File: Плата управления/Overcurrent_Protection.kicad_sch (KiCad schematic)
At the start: 10 parts, among them U5 INA283, U5 LMV7239M5

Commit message: VER2.0
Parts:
- U5: value INA283 -> INA282
- U5: footprint Package_TO_SOT_SMD:SOT-353_SC-70-5 -> Package_TO_SOT_SMD:SOT-23-5_HandSoldering
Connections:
- net +3.3V: no longer U5.3 (REF2)
- net GND: now also U5.3 (REF2)
- net Shunt_1 renamed Shunt-
- net Shunt_2 renamed Shunt+
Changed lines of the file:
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@@
     (effects (font (size 2.5 2.5) bold) (justify left bottom))
   )
-  (global_label "Shunt_1" (shape input) (at 121.285 113.03 180) (fields_autoplaced)
+  (global_label "Shunt-" (shape input) (at 121.285 113.03 180) (fields_autoplaced)
     (effects (font (size 1.27 1.27)) (justify right))
-    (property "Intersheetrefs" "${INTERSHEET_REFS}" (at 110.8199 113.03 0)
+    (property "Intersheetrefs" "${INTERSHEET_REFS}" (at 113.1833 113.03 0)
       (effects (font (size 1.27 1.27)) (justify right) hide)
     )
   )
-  (global_label "Shunt_2" (shape input) (at 121.285 107.95 180) (fields_autoplaced)
+  (global_label "Shunt+" (shape input) (at 121.285 107.95 180) (fields_autoplaced)
     (effects (font (size 1.27 1.27)) (justify right))
-    (property "Intersheetrefs" "${INTERSHEET_REFS}" (at 110.8199 107.95 0)
+    (property "Intersheetrefs" "${INTERSHEET_REFS}" (at 113.1833 107.95 0)
       (effects (font (size 1.27 1.27)) (justify right) hide)
     )
@@
     )
   )
+  (symbol (lib_id "power:GND") (at 128.905 119.38 0) (unit 1)
+    (in_bom yes) (on_board yes) (dnp no) (fields_autoplaced)
+    (property "Reference" "#PWR047" (at 128.905 125.73 0)
+      (effects (font (size 1.27 1.27)) hide)
+    )
+    (property "Value" "GND" (at 128.905 124.46 0)
+      (effects (font (size 1.27 1.27)))
+    )
+    (property "Footprint" "" (at 128.905 119.38 0)
+      (effects (font (size 1.27 1.27)) hide)
+    )
+    (property "Datasheet" "" (at 128.905 119.38 0)
+      (effects (font (size 1.27 1.27)) hide)
+    )
+    (pin "1")
+    (instances
+      (project "Плата управления"
+        (path "/75f4c67c-bbde-4446-8f82-67797a1b269f/d6b8b9ce-300b-4d22-9d4c-9182eba581b1"
+          (reference "#PWR047") (unit 1)
+        )
+        (path "/75f4c67c-bbde-4446-8f82-67797a1b269f/c91ff3ec-ad20-4326-acd4-2c9dea437172"
+          (reference "#PWR021") (unit 1)
+        )
+      )
+      (project "Силовая плата"
+        (path "/96c6fc92-8ec6-44f7-b0dc-9ad8f1acea09"
+          (reference "#PWR06") (unit 1)
+        )
+        (path "/96c6fc92-8ec6-44f7-b0dc-9ad8f1acea09/1efb5faf-bb82-4ac6-a144-d6576b4720aa"
+          (reference "#PWR015") (unit 1)
+        )
+        (path "/96c6fc92-8ec6-44f7-b0dc-9ad8f1acea09/a27b443f-c036-4fd6-934c-6ea912709de0"
+          (reference "#PWR025") (unit 1)
+        )
+      )
+    )
+  )
   (symbol (lib_id "Amplifier_Current:INA283") (at 128.905 110.49 0) (unit 1)
     (in_bom yes) (on_board yes) (dnp no)
@@
       (effects (font (size 1.27 1.27)))
     )
-    (property "Value" "INA283" (at 133.985 107.95 0)
+    (property "Value" "INA282" (at 133.985 107.95 0)
       (effects (font (size 1.27 1.27)))
     )
@@
     )
   )
-  (symbol (lib_id "power:+3.3V") (at 128.905 119.38 180) (unit 1)
-    (in_bom yes) (on_board yes) (dnp no) (fields_autoplaced)
-    (property "Reference" "#PWR025" (at 128.905 115.57 0)
-      (effects (font (size 1.27 1.27)) hide)
-    )
-    (property "Value" "+3.3V" (at 128.905 124.46 0)
-      (effects (font (size 1.27 1.27)))
-    )
-    (property "Footprint" "" (at 128.905 119.38 0)
-      (effects (font (size 1.27 1.27)) hide)
-    )
-    (property "Datasheet" "" (at 128.905 119.38 0)
-      (effects (font (size 1.27 1.27)) hide)
-    )
-    (pin "1")
-    (instances
-      (project "Плата управления"
-        (path "/75f4c67c-bbde-4446-8f82-67797a1b269f/d6b8b9ce-300b-4d22-9d4c-9182eba581b1"
-          (reference "#PWR025") (unit 1)
-        )
-        (path "/75f4c67c-bbde-4446-8f82-67797a1b269f/c91ff3ec-ad20-4326-acd4-2c9dea437172"
-          (reference "#PWR021") (unit 1)
-        )
-      )
-    )
-  )
   (symbol (lib_id "power:GND") (at 123.825 119.38 0) (unit 1)
     (in_bom yes) (on_board yes) (dnp no) (fields_autoplaced)
@@
       (effects (font (size 1.27 1.27)))
     )
-    (property "Footprint" "Package_TO_SOT_SMD:SOT-353_SC-70-5" (at 169.545 113.03 0)
+    (property "Footprint" "Package_TO_SOT_SMD:SOT-23-5_HandSoldering" (at 169.545 113.03 0)
       (effects (font (size 1.27 1.27)) (justify left) hide)
     )

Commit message: Добавил NTC обработку
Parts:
- renumbered C16 to C10, C17 to C7, C16 to C8, C18 to C9, R29 to R13, R29 to R14, R30 to R15, R29 to R16, U5 to U4

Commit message: Новые драйвера и разъёмы
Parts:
- U5: value INA282 -> AD8418A
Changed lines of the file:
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@@
 			)
 		)
-		(property "Value" "INA282"
-			(at 133.985 107.95 0)
+		(property "Value" "AD8418A"
+			(at 133.858 107.188 0)
 			(effects
 				(font

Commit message: Развел все длорожки
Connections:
- net Enable renamed PWM_BKIN
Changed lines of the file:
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@@
+		)
+	)
+	(global_label "PWM_BKIN"
+		(shape output)
+		(at 191.135 107.95 0)
+		(fields_autoplaced yes)
+		(effects
+			(font
+				(size 1.27 1.27)
+			)
+			(justify left)
+		)
+		(property "Intersheetrefs" "${INTERSHEET_REFS}"
+			(at 203.7359 107.95 0)
+			(effects
+				(font
+					(size 1.27 1.27)
+				)
+				(justify left)
+				(hide yes)
+			)
 		)
 	)
@@
 				(hide yes)
 			)
-		)
-	)
-	(global_label "Enable"
-		(shape output)
-		(at 191.135 107.95 0)
-		(fields_autoplaced yes)
-		(effects
-			(font
-				(size 1.27 1.27)
-			)
-			(justify left)
-		)
-		(property "Intersheetrefs" "${INTERSHEET_REFS}"
-			(at 200.47 107.95 0)
-			(effects
-				(font
-					(size 1.27 1.27)
-				)
-				(justify left)
-				(hide yes)
-			)

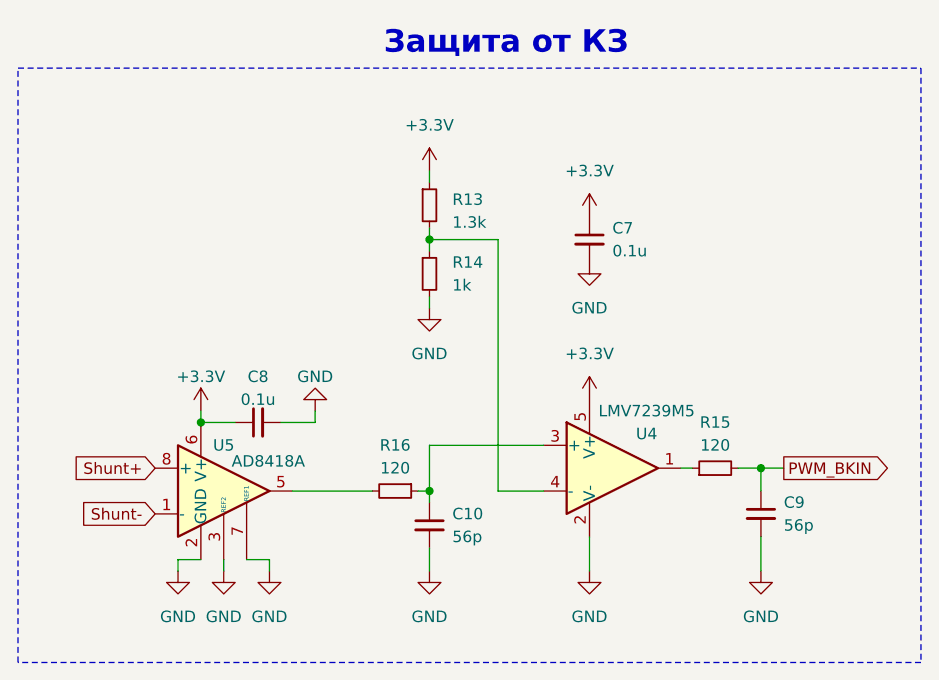
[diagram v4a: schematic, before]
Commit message: Добавил все в BOM
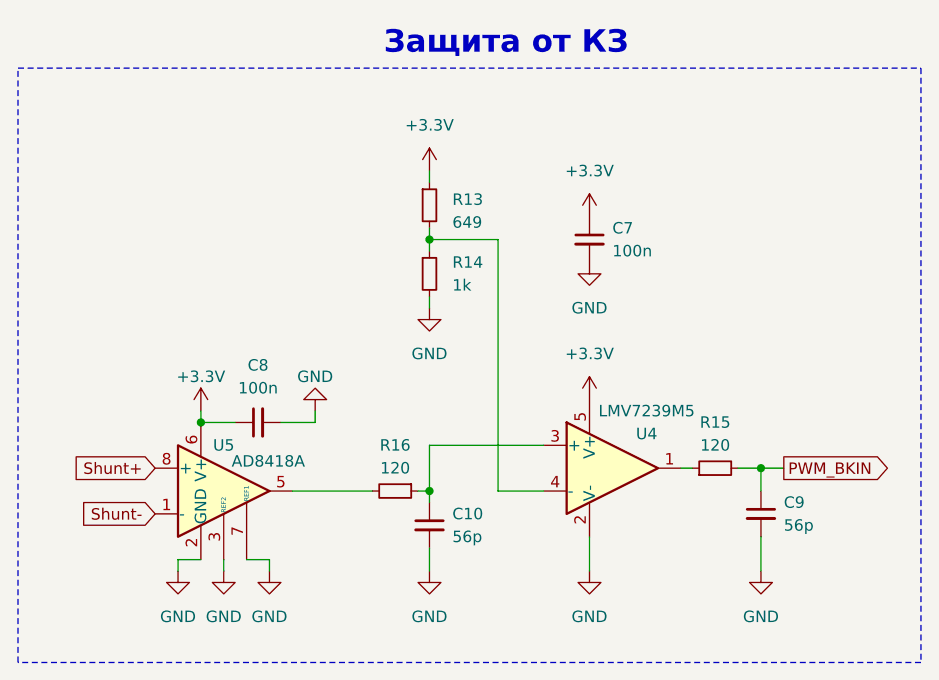
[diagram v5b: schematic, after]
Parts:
- C7, C8: value 0.1u -> 100n
- R13: value 1.3k -> 649
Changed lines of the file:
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@@
 			)
 		)
-		(property "Value" "0.1u"
+		(property "Value" "100n"
 			(at 172.085 83.8263 0)
 			(effects
@@
 			)
 		)
-		(property "Value" "1.3k"
+		(property "Value" "649"
 			(at 154.305 80.645 0)
 			(effects
@@
 		(fields_autoplaced yes)
 		(property "Reference" "C8"
-			(at 132.7213 97.79 90)
-			(effects
-				(font
-					(size 1.27 1.27)
-				)
-			)
-		)
-		(property "Value" "0.1u"
-			(at 132.7213 100.33 90)
-			(effects
-				(font
+			(at 132.7213 96.52 90)
+			(effects
+				(font
+					(size 1.27 1.27)
+				)
+			)
+		)
+		(property "Value" "100n"
+			(at 132.7213 99.06 90)
+			(effects
+				(font
